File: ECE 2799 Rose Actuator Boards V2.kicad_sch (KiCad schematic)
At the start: 2 parts, among them U1 ESP32-C6-MINI-1

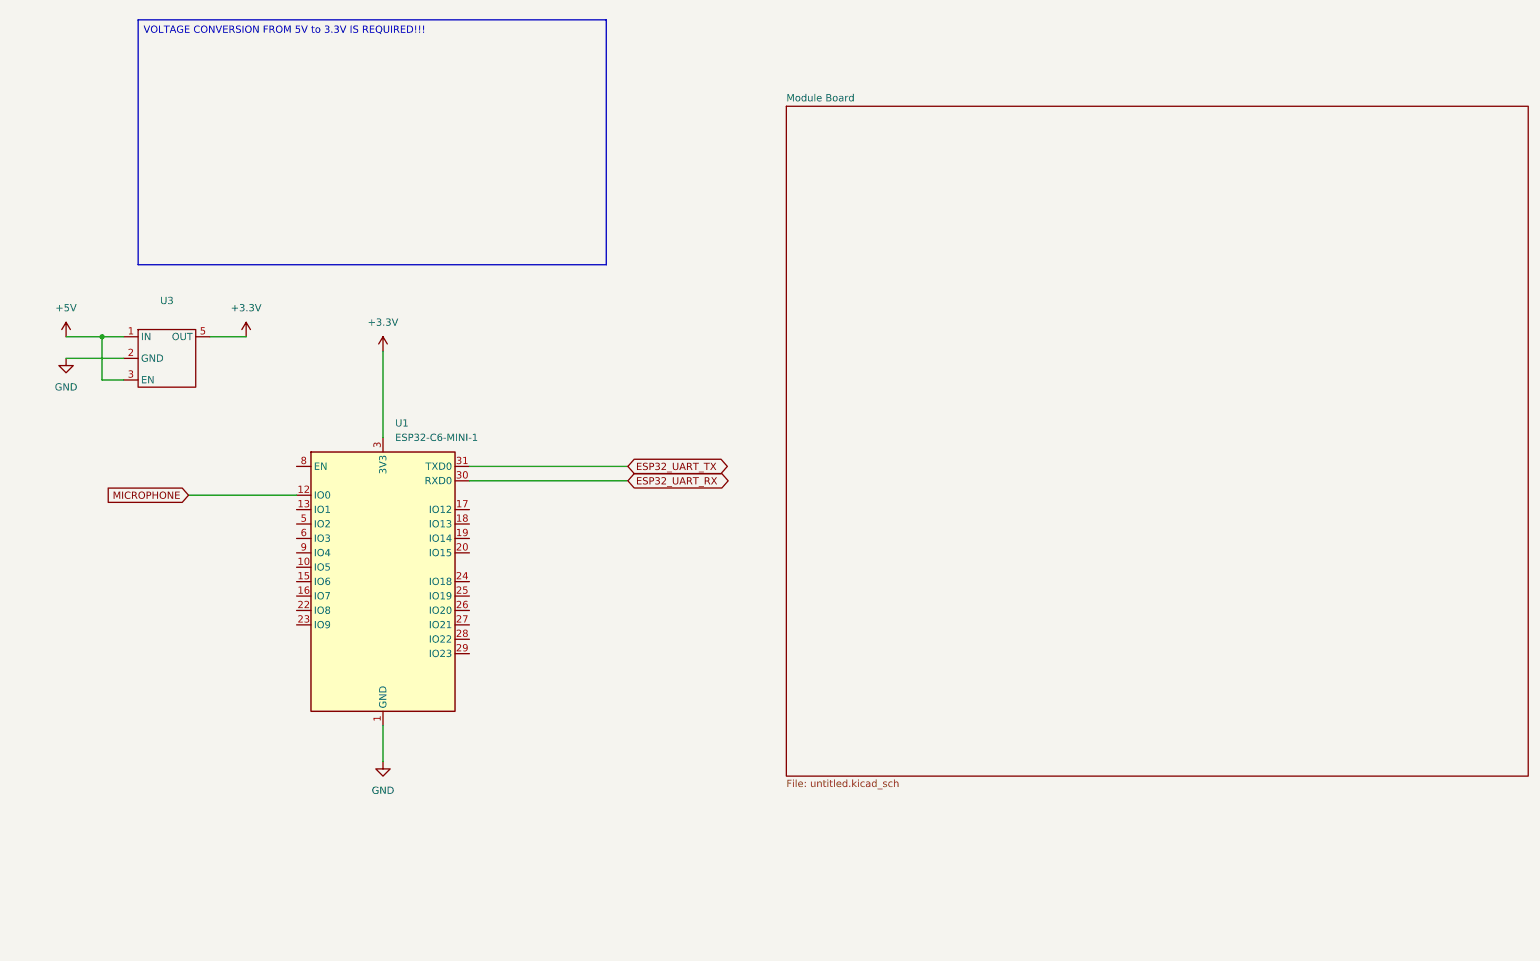
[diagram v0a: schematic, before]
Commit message: Fixed things, added microphone amplifier, ...
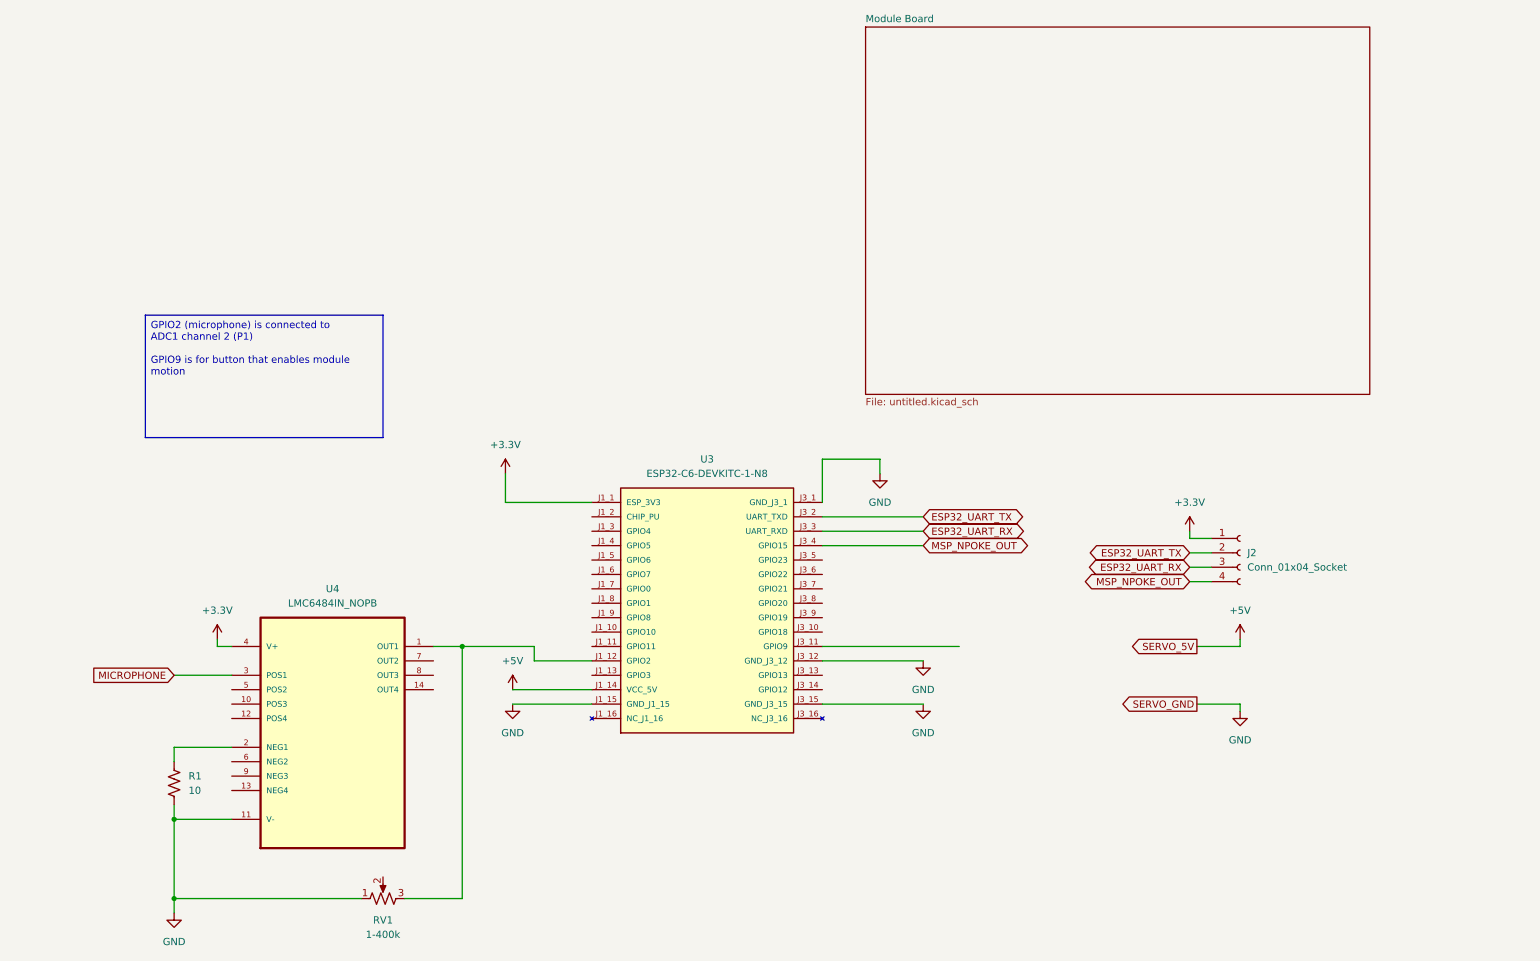
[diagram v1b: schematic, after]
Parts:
- removed U1: ESP32-C6-MINI-1, RF_Module:ESP32-C6-MINI-1, symbol RF_Module:ESP32-C6-MINI-1
- removed U3: ~, symbol roseActuatorLibrary:TLV78533PDBVR
- added J2: Conn_01x04_Socket, symbol Connector:Conn_01x04_Socket
- added R1: 10, symbol Device:R_US
- added RV1: 1-400k, symbol Device:R_Potentiometer_US
- added U3: ESP32-C6-DEVKITC-1-N8, ESP32-C6-DEVKITC-1-N8:MODULE_ESP32-C6-DEVKITC-1-N8, symbol roseActuatorLibrary:ESP32-C6-DEVKITC-1-N8
- added U4: LMC6484IN_NOPB, LMC6484IN_NOPB:DIP254P762X508-14, symbol roseActuatorLibrary:LMC6484IN_NOPB
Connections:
- net +3.3V: now also J2.1 (Pin_1), U3.J1_1 (ESP_3V3), U4.4 (V+)
- net +5V: now also U3.J1_14 (VCC_5V)
- net ESP32_UART_RX: now also J2.3 (Pin_3), U3.J3_3 (UART_RXD)
- net ESP32_UART_TX: now also J2.2 (Pin_2), U3.J3_2 (UART_TXD)
- net GND: now also R1.2, RV1.1, U3.J1_15 (GND_J1_15), U3.J3_1 (GND_J3_1), U3.J3_12 (GND_J3_12), U3.J3_15 (GND_J3_15), U4.11 (V-)
- net MICROPHONE: now also U4.3 (POS1)
- new net: RV1.3, U3.J1_12 (GPIO2), U4.1 (OUT1)
- new net: R1.1, U4.2 (NEG1)
- new net MSP_NPOKE_OUT: J2.4 (Pin_4), U3.J3_4 (GPIO15)

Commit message: Fixed amplifier resistors, fixed potentiometer
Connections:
- net GND: now also RV1.3; no longer RV1.1
- net at U3.J1_12 (GPIO2), U4.1 (OUT1): now also RV1.2; no longer RV1.3
- net at R1.1, U4.2 (NEG1): now also RV1.1
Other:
- moved on the sheet: J2, R1, RV1, U3, U4

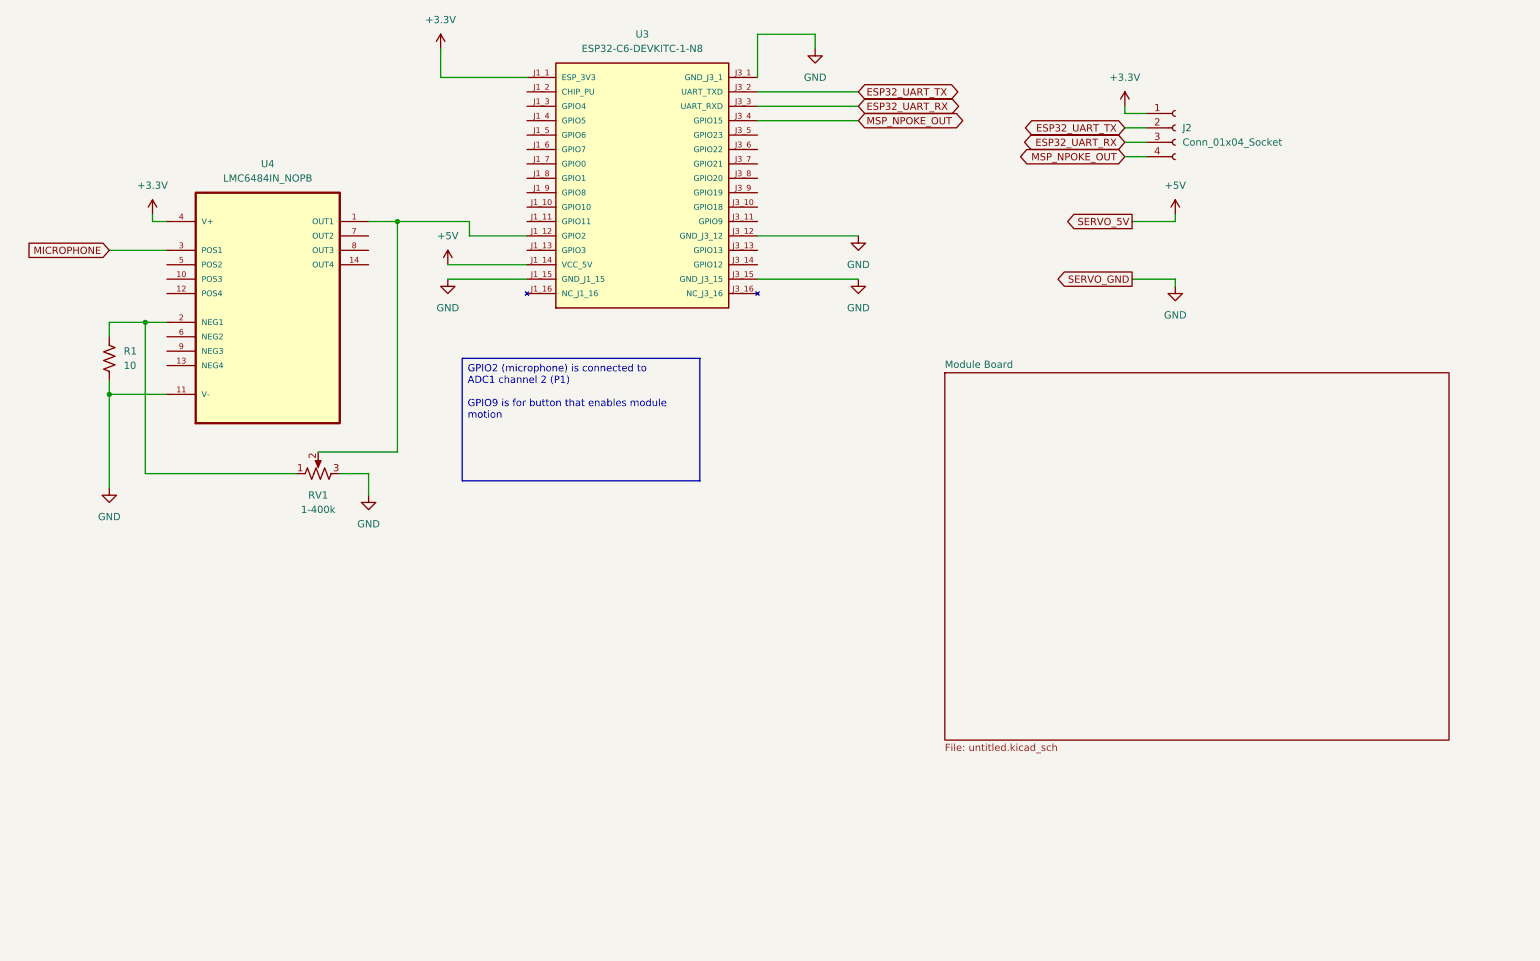
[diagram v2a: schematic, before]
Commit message: schem Rev 1 Ready for layout
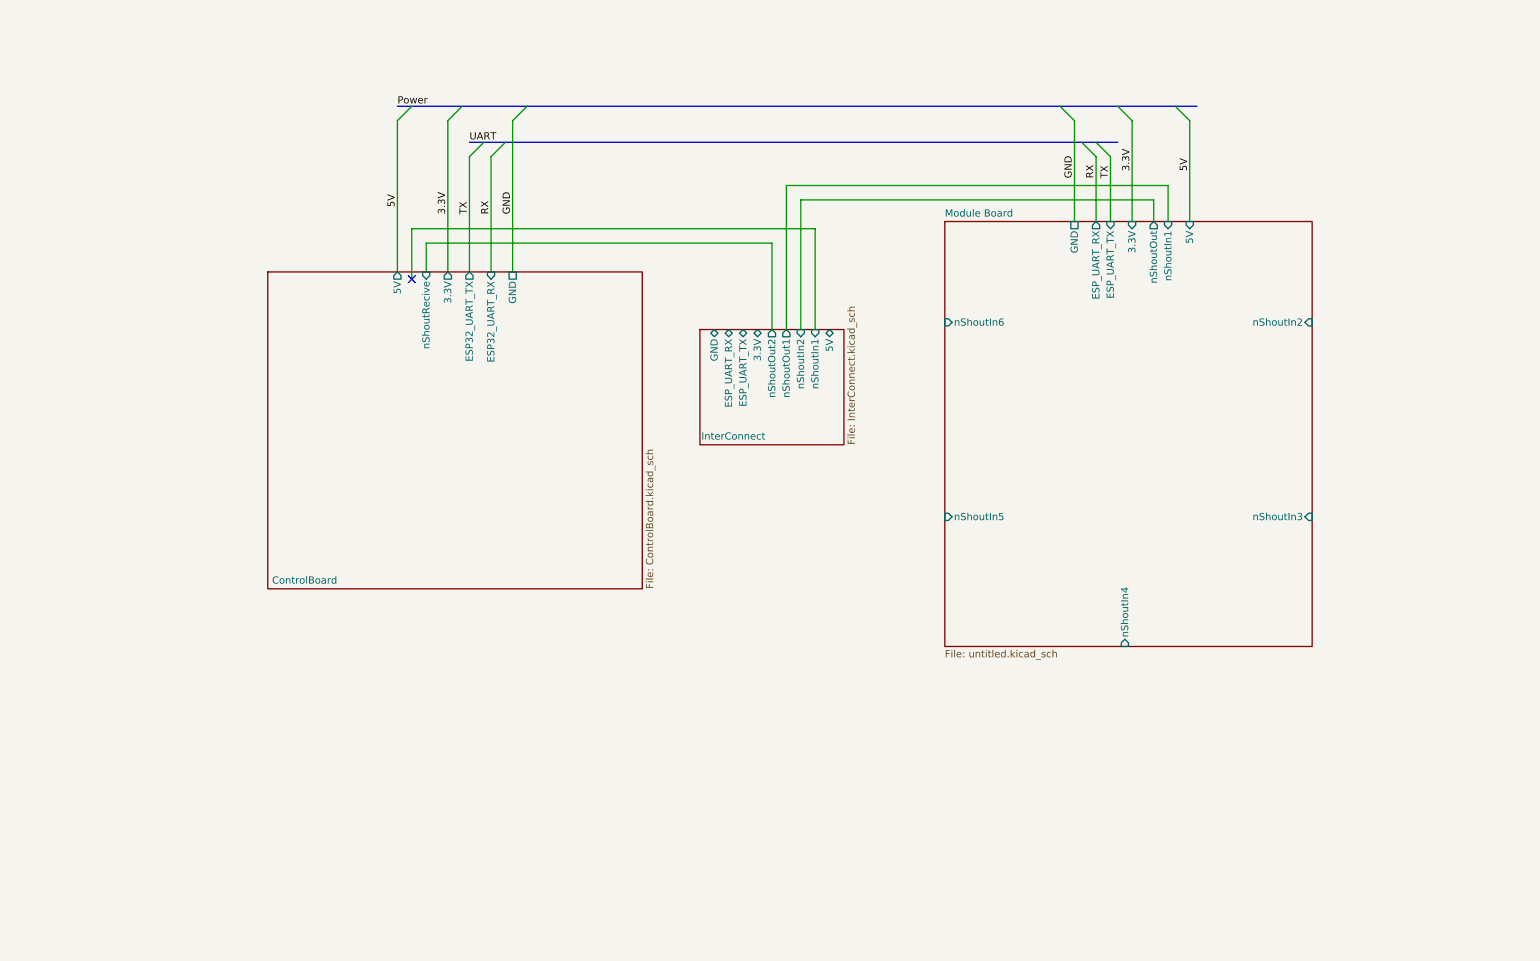
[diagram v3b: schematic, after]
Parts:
- removed J2: Conn_01x04_Socket, symbol Connector:Conn_01x04_Socket
- removed R1: 10, symbol Device:R_US
- removed RV1: 1-400k, symbol Device:R_Potentiometer_US
- removed U3: ESP32-C6-DEVKITC-1-N8, ESP32-C6-DEVKITC-1-N8:MODULE_ESP32-C6-DEVKITC-1-N8, symbol roseActuatorLibrary:ESP32-C6-DEVKITC-1-N8
- removed U4: LMC6484IN_NOPB, LMC6484IN_NOPB:DIP254P762X508-14, symbol roseActuatorLibrary:LMC6484IN_NOPB
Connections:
- no-connect marks 0 -> 1
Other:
- added sheet ControlBoard (ControlBoard.kicad_sch)
- added sheet InterConnect (InterConnect.kicad_sch)
- sheet Module Board ports: added 3.3V, 5V, ESP_UART_RX, ESP_UART_TX, GND, nShoutIn1, nShoutIn2, nShoutIn3, nShoutIn4, nShoutIn5, nShoutIn6, nShoutOut; removed none
- company: (none) -> WPI
- title: (none) -> Basic Connections

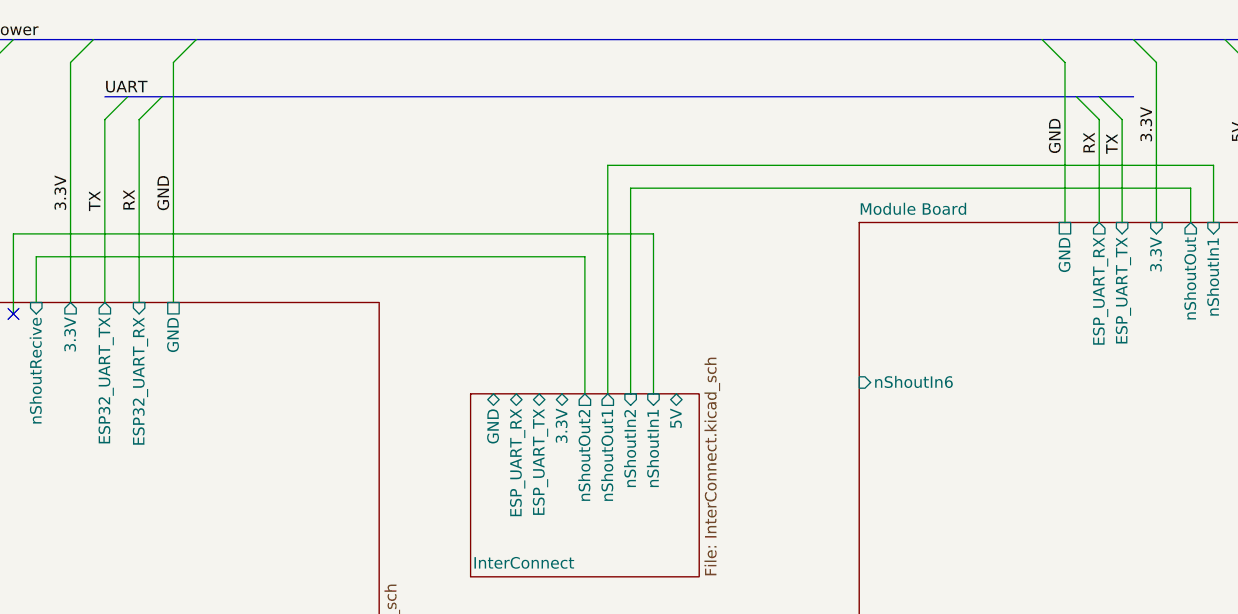
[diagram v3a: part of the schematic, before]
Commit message: Refrences Changed, Root file fixed, UART Note Added
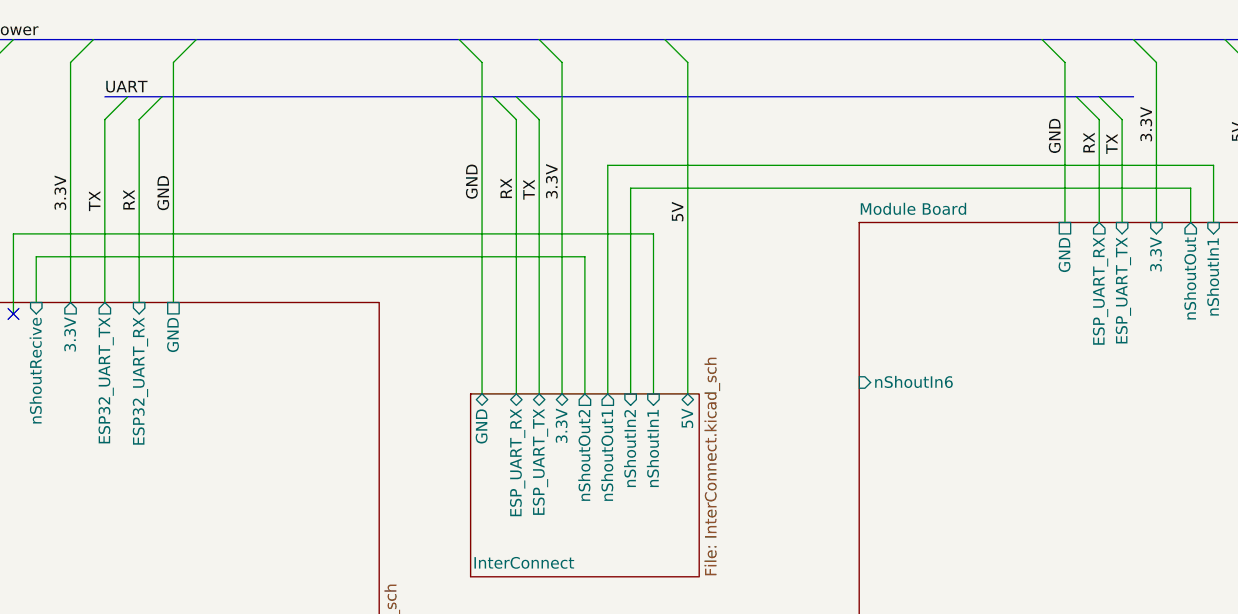
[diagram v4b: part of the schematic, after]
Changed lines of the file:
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@@
+	)
+	(bus_entry
+		(at 132.08 38.1)
+		(size 2.54 2.54)
+		(stroke
+			(width 0)
+			(type default)
+		)
+	)
+	(bus_entry
+		(at 140.97 38.1)
+		(size 2.54 2.54)
+		(stroke
+			(width 0)
+			(type default)
+		)
 	)
 	(bus_entry
@@
 	)
 	(bus_entry
+		(at 138.43 44.45)
+		(size 2.54 2.54)
+		(stroke
+			(width 0)
+			(type default)
+		)
+	)
+	(bus_entry
 		(at 207.01 38.1)
 		(size 2.54 2.54)
@@
 	)
 	(bus_entry
+		(at 135.89 44.45)
+		(size 2.54 2.54)
+		(stroke
+			(width 0)
+			(type default)
+		)
+	)
+	(bus_entry
 		(at 217.17 38.1)
+		(size 2.54 2.54)
+		(stroke
+			(width 0)
+			(type default)
+		)
+	)
+	(bus_entry
+		(at 154.94 38.1)
 		(size 2.54 2.54)
 		(stroke
@@
 	(wire
 		(pts
+			(xy 134.62 40.64) (xy 134.62 77.47)
+		)
+		(stroke
+			(width 0)
+			(type default)
+		)
+	)
+	(wire
+		(pts
 			(xy 146.05 62.23) (xy 146.05 77.47)
 		)
@@
 		)
 	)
+	(bus
+		(pts
+			(xy 138.43 44.45) (xy 200.66 44.45)
+		)
+		(stroke
+			(width 0)
+			(type default)
+		)
+	)
 	(wire
 		(pts
@@
 		)
 	)
-	(bus
-		(pts
-			(xy 102.87 38.1) (xy 196.85 38.1)
+	(wire
+		(pts
+			(xy 140.97 46.99) (xy 140.97 77.47)
+		)
+		(stroke
+			(width 0)
+			(type default)
+		)
+	)
+	(bus
+		(pts
+			(xy 135.89 44.45) (xy 138.43 44.45)
+		)
+		(stroke
+			(width 0)
+			(type default)
+		)
+	)
+	(bus
+		(pts
+			(xy 102.87 38.1) (xy 132.08 38.1)
 		)
 		(stroke
@@
 		)
 	)
+	(bus
+		(pts
+			(xy 132.08 38.1) (xy 140.97 38.1)
+		)
+		(stroke
+			(width 0)
+			(type default)
+		)
+	)
 	(wire
 		(pts
@@
 	(bus
 		(pts
+			(xy 140.97 38.1) (xy 154.94 38.1)
+		)
+		(stroke
+			(width 0)
+			(type default)
+		)
+	)
+	(bus
+		(pts
 			(xy 217.17 38.1) (xy 220.98 38.1)
 		)
@@
 		)
 	)
-	(bus
-		(pts
-			(xy 99.06 44.45) (xy 200.66 44.45)
+	(wire
+		(pts
+			(xy 157.48 40.64) (xy 157.48 77.47)
+		)
+		(stroke
+			(width 0)
+			(type default)
+		)
+	)
+	(wire
+		(pts
+			(xy 143.51 40.64) (xy 143.51 77.47)
+		)
+		(stroke
+			(width 0)
+			(type default)
+		)
+	)
+	(bus
+		(pts
+			(xy 99.06 44.45) (xy 135.89 44.45)
 		)
 		(stroke
@@
 	(bus
 		(pts
+			(xy 154.94 38.1) (xy 196.85 38.1)
+		)
+		(stroke
+			(width 0)
+			(type default)
+		)
+	)
+	(bus
+		(pts
 			(xy 91.44 38.1) (xy 102.87 38.1)
 		)
@@
 		(pts
 			(xy 200.66 44.45) (xy 203.2 44.45)
+		)
+		(stroke
+			(width 0)
+			(type default)
+		)
+	)
+	(wire
+		(pts
+			(xy 138.43 46.99) (xy 138.43 77.47)
 		)
 		(stroke
@@
 		)
 	)
+	(label "3.3V"
+		(at 143.51 55.88 90)
+		(effects
+			(font
+				(size 1.27 1.27)
+			)
+			(justify left bottom)
+		)
+	)
+	(label "5V"
+		(at 157.48 58.42 90)
+		(effects
+			(font
+				(size 1.27 1.27)
+			)
+			(justify left bottom)
+		)
+	)
 	(label "TX"
 		(at 205.74 50.8 90)
@@
 		)
 	)
+	(label "TX"
+		(at 140.97 55.88 90)
+		(effects
+			(font
+				(size 1.27 1.27)
+			)
+			(justify left bottom)
+		)
+	)
 	(label "GND"
 		(at 199.39 50.8 90)
@@
 		)
 	)
+	(label "RX"
+		(at 138.43 55.88 90)
+		(effects
+			(font
+				(size 1.27 1.27)
+			)
+			(justify left bottom)
+		)
+	)
 	(label "3.3V"
 		(at 88.9 57.15 90)
@@
 	(label "5V"
 		(at 219.71 49.53 90)
+		(effects
+			(font
+				(size 1.27 1.27)
+			)
+			(justify left bottom)
+		)
+	)
+	(label "GND"
+		(at 134.62 55.88 90)
 		(effects
 			(font
@@
 		)
 		(pin "GND" bidirectional
-			(at 135.89 77.47 90)
+			(at 134.62 77.47 90)
 			(effects
 				(font
@@
 		)
 		(pin "5V" bidirectional
-			(at 156.21 77.47 90)
+			(at 157.48 77.47 90)
 			(effects
 				(font
